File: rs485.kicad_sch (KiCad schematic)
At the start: 36 parts, among them J1801 RS485 RX Socket, J1802 RS485 TX Socket, U1804 ISO7721DR, U1805 SN75176BDR, U1806 SN75176BDR

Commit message: Weeded out all ERC errors
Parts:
- removed R1801: 330R, PCM_Resistor_SMD_AKL:R_0402_1005Metric, symbol Device:R
- C1801, C1803, C1805, C1807: footprint PCM_Capacitor_SMD_AKL:C_0603_1608Metric -> Capacitor_SMD:C_0603_1608Metric
- C1802, C1806: footprint PCM_Capacitor_SMD_AKL:C_0402_1005Metric -> Capacitor_SMD:C_0402_1005Metric
- C1808: renamed from C1810; footprint PCM_Capacitor_SMD_AKL:C_0603_1608Metric -> Capacitor_SMD:C_0603_1608Metric
- C1809: renamed from C1811; footprint PCM_Capacitor_SMD_AKL:C_0603_1608Metric -> Capacitor_SMD:C_0603_1608Metric
- C1810: renamed from C1812; footprint PCM_Capacitor_SMD_AKL:C_0603_1608Metric -> Capacitor_SMD:C_0603_1608Metric
- C1811: renamed from C1813; footprint PCM_Capacitor_SMD_AKL:C_0603_1608Metric -> Capacitor_SMD:C_0603_1608Metric
- C1812: renamed from C1808; footprint PCM_Capacitor_SMD_AKL:C_0402_1005Metric -> Capacitor_SMD:C_0402_1005Metric
- C1813: renamed from C1809; footprint PCM_Capacitor_SMD_AKL:C_0402_1005Metric -> Capacitor_SMD:C_0402_1005Metric
- R1801: renamed from R1802; footprint PCM_Resistor_SMD_AKL:R_0402_1005Metric -> Resistor_SMD:R_0402_1005Metric
- R1802: renamed from R1803; footprint PCM_Resistor_SMD_AKL:R_0402_1005Metric -> Resistor_SMD:R_0402_1005Metric
- R1803: renamed from R1804; footprint PCM_Resistor_SMD_AKL:R_0402_1005Metric -> Resistor_SMD:R_0402_1005Metric
- R1804: renamed from R1805; footprint PCM_Resistor_SMD_AKL:R_0402_1005Metric -> Resistor_SMD:R_0402_1005Metric
- U1801: renamed from U1804; LCSC (none) -> C366164
- renumbered U1805 to U1802, U1806 to U1803
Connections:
- net +3.3V renamed CMx_3V3
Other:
- note removed: "Dummy load to help with voltage regulation"
- company: Nabu Casa -> Hat Labs Oy
- title: Overview -> HALPI2

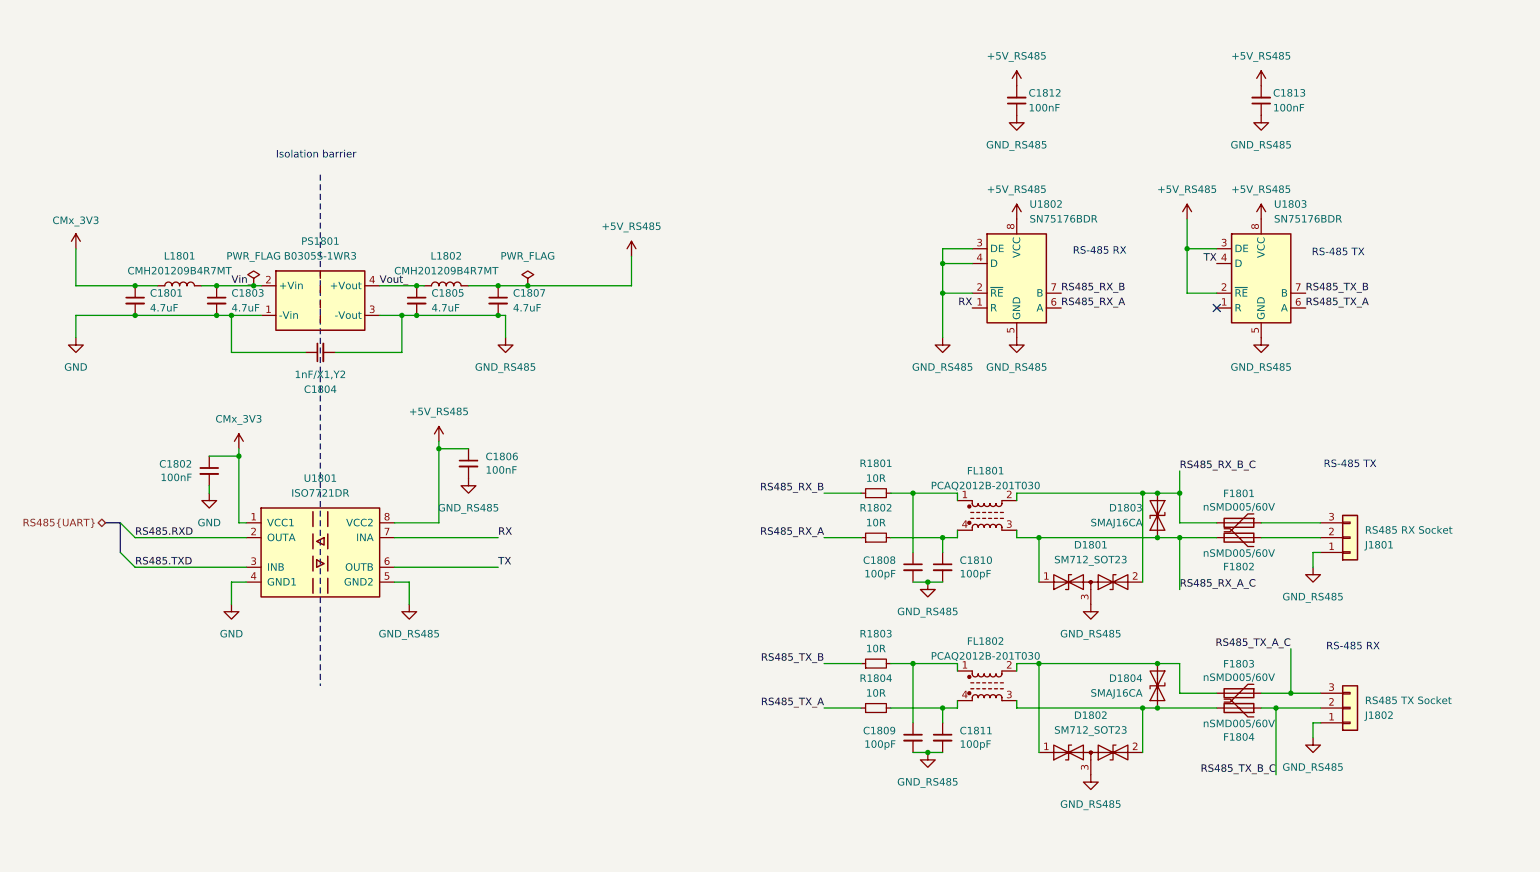
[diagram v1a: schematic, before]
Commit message: Implement ideal diodes for input and LDO power ORing
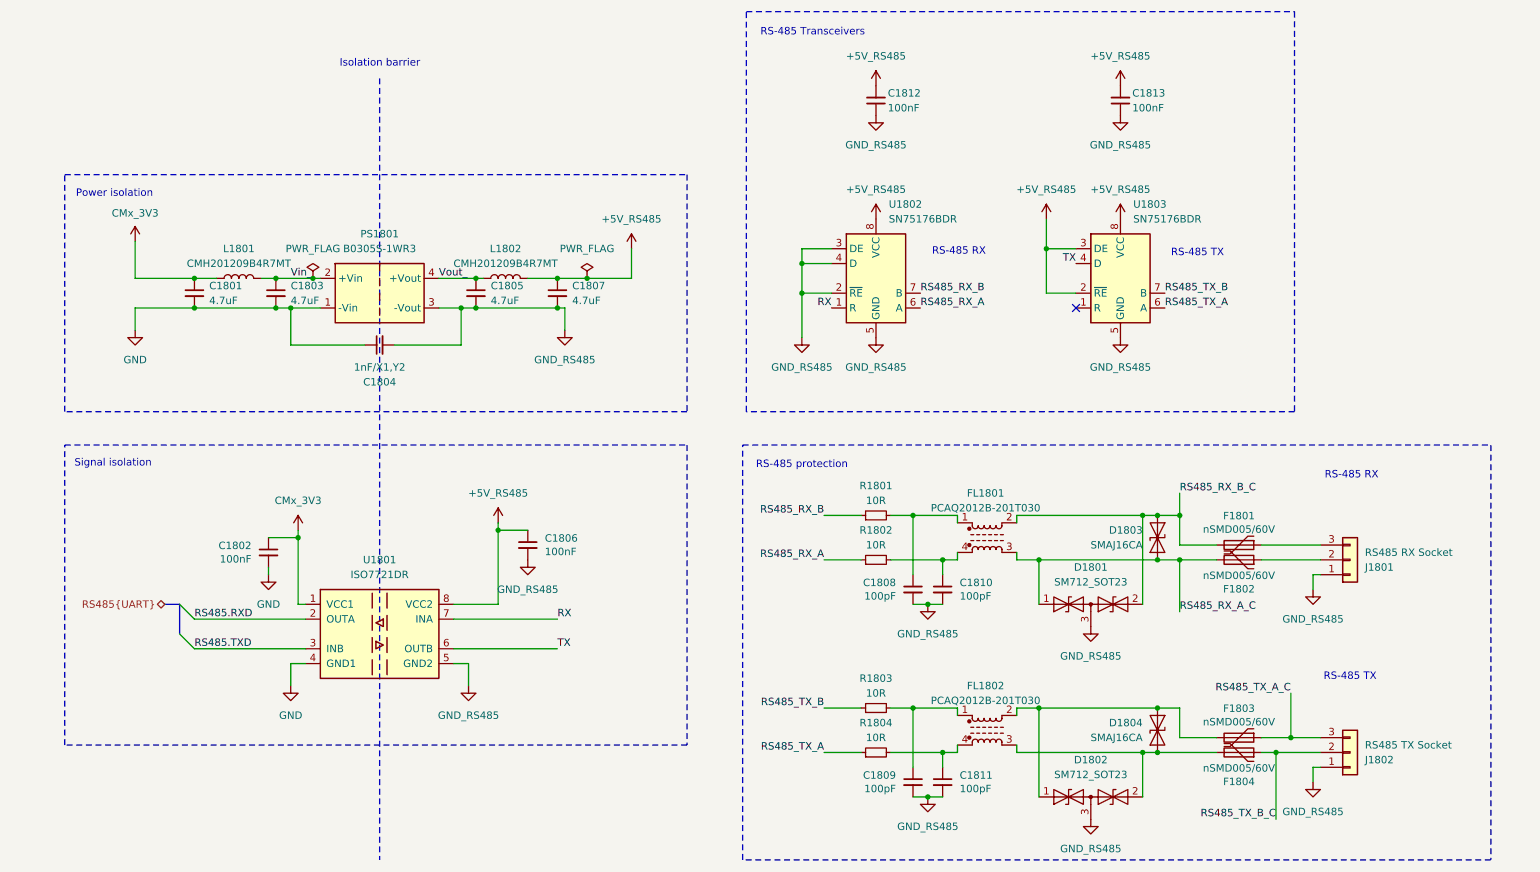
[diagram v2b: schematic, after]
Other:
- note added: "Power isolation"
- note added: "RS-485 Transceivers"
- note added: "RS-485 protection"
- note added: "Signal isolation"
- moved on the sheet: C1801, C1802, C1803, C1804, C1805, C1806, C1807, C1808, C1809, C1810, C1811, C1812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

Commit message: Re-annotate schematics
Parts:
- renumbered C1812 to C1808, C1808 to C1809, C1809 to C1810, C1810 to C1811, C1811 to C1812

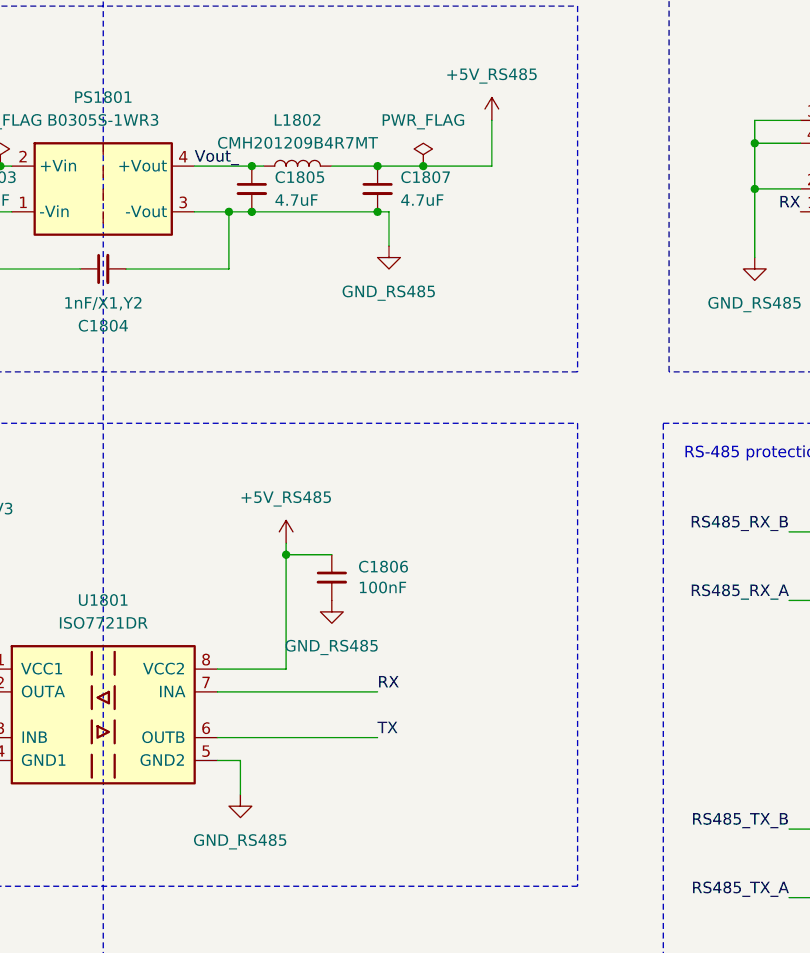
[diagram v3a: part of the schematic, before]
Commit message: Sprinkle test points on the schematics
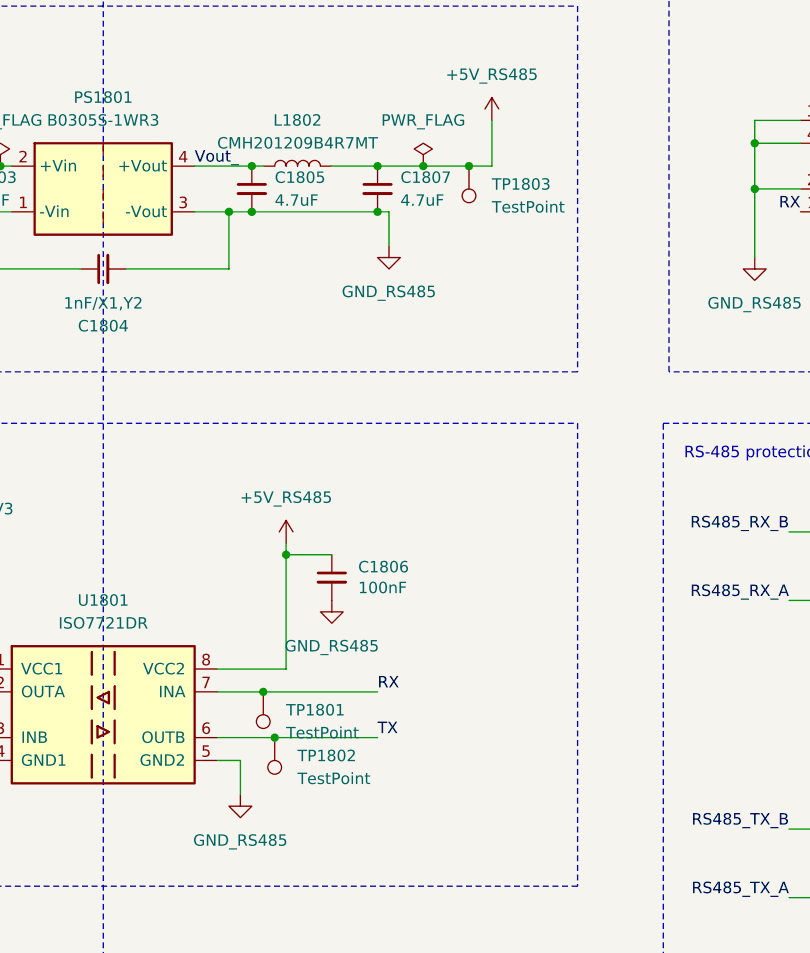
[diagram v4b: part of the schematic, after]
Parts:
- added TP1801, TP1802, TP1803: TestPoint, TestPoint:TestPoint_Pad_D1.0mm, symbol Connector:TestPoint
- C1804: footprint HALSER:C_1808_4520Metric -> Hatlabs:C_1808_4520Metric
- FL1801, FL1802: footprint HALSER:L_CommonModeChoke_PCAQ2012B -> Hatlabs:L_CommonModeChoke_PCAQ2012B
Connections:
- net +5V_RS485: now also TP1803.1
- net RX: now also TP1801.1
- net TX: now also TP1802.1

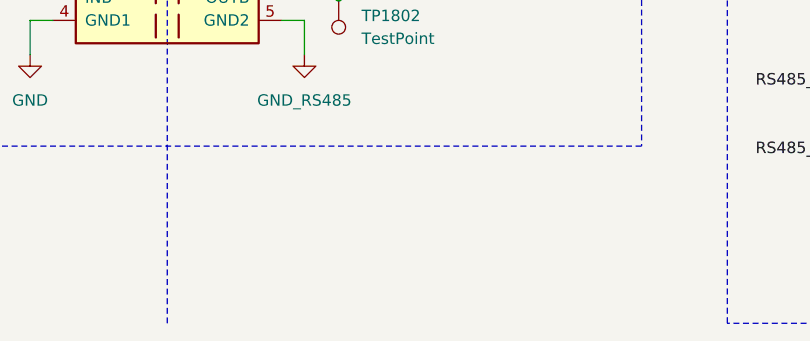
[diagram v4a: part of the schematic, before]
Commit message: Revert USB3 ports back to Type A
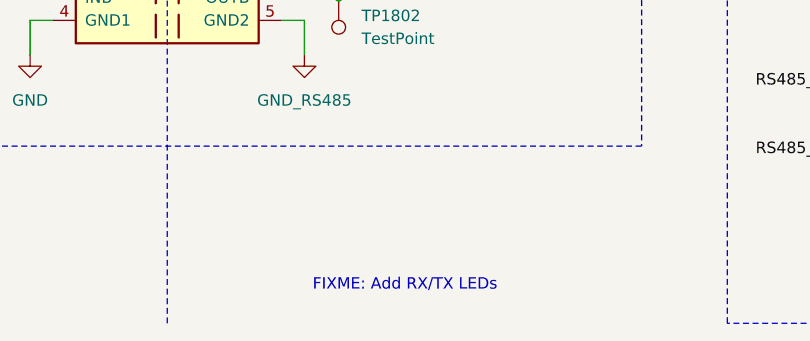
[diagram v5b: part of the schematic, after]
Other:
- note added: "FIXME: Add RX/TX LEDs"
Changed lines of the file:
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@@
+		)
+	)
+	(text "FIXME: Add RX/TX LEDs"
+		(exclude_from_sim no)
+		(at 101.346 157.734 0)
+		(effects
+			(font
+				(size 1.27 1.27)
+				(color 255 0 0 1)
+			)
 		)
 	)

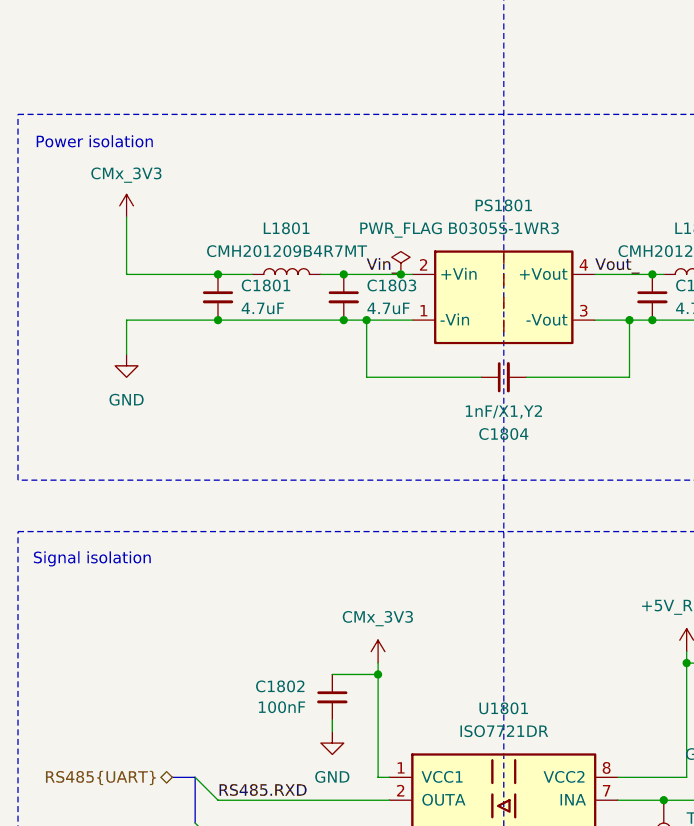
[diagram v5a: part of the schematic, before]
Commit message: Implement a USB3 hub
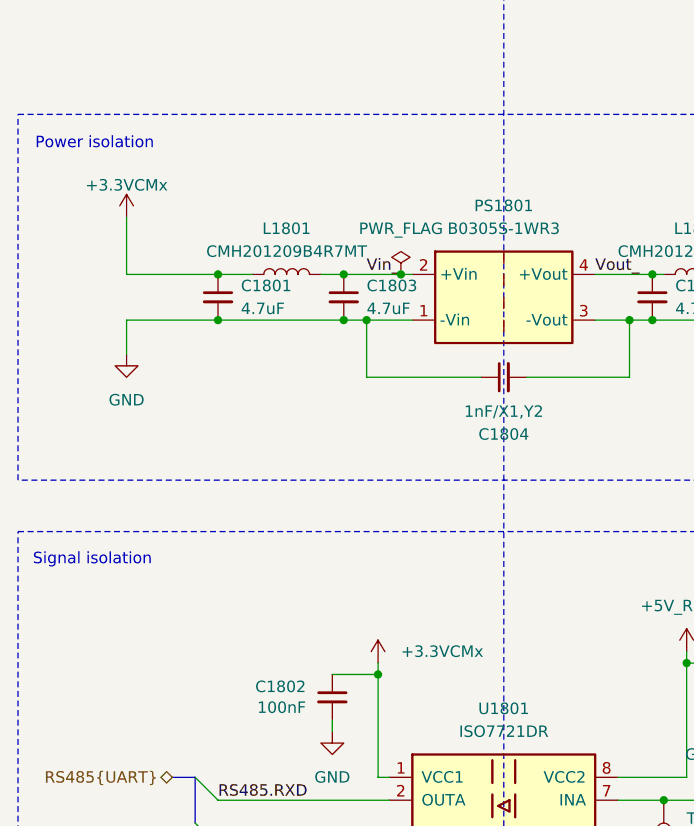
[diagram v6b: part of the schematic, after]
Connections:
- net CMx_3V3 renamed +3.3VCMx
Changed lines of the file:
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@@
 			)
 		)
+		(property "Sim.Enable" ""
+			(at 93.98 125.73 0)
+			(effects
+				(font
+					(size 1.27 1.27)
+				)
+				(hide yes)
+			)
+		)
 		(pin "1"
 		)
@@
 			)
 		)
+		(property "Sim.Enable" ""
+			(at 115.57 62.23 0)
+			(effects
+				(font
+					(size 1.27 1.27)
+				)
+				(hide yes)
+			)
+		)
 		(pin "1"
 		)
@@
 			)
 		)
+		(property "Sim.Enable" ""
+			(at 92.71 120.65 0)
+			(effects
+				(font
+					(size 1.27 1.27)
+				)
+				(hide yes)
+			)
+		)
 		(pin "1"
 		)
@@
 	)
 	(symbol
-		(lib_id "power:+3V3")
+		(lib_id "Hatlabs:+3.3VCMx")
 		(at 33.02 55.88 0)
 		(unit 1)
@@
 			)
 		)
-		(property "Value" "CMx_3V3"
-			(at 33.02 51.054 0)
+		(property "Value" "+3.3VCMx"
+			(at 33.02 52.324 0)
 			(effects
 				(font
@@
 			)
 		)
-		(property "Description" "Power symbol creates a global label with name \"+3V3\""
+		(property "Description" "Power symbol driven by the CMx module +3.3V output"
 			(at 33.02 55.88 0)
 			(effects
@@
 	)
 	(symbol
-		(lib_id "power:+3V3")
+		(lib_id "Hatlabs:+3.3VCMx")
 		(at 60.96 105.41 0)
 		(unit 1)
@@
 			)
 		)
-		(property "Value" "CMx_3V3"
-			(at 60.96 100.33 0)
+		(property "Value" "+3.3VCMx"
+			(at 63.5 104.1399 0)
 			(effects
 				(font
 					(size 1.27 1.27)
 				)
+				(justify left)
 			)
 		)
@@
 			)
 		)
-		(property "Description" "Power symbol creates a global label with name \"+3V3\""
+		(property "Description" "Power symbol driven by the CMx module +3.3V output"
 			(at 60.96 105.41 0)
 			(effects
